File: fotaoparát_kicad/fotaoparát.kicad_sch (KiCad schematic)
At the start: 43 parts, among them J1 Conn_01x01_Pin, J10 Conn_01x01_Pin, J11 Conn_01x01_Pin, J12 Conn_01x01_Pin, J13 USB_C_Receptacle_USB2.0_16P, J2 Conn_01x01_Pin, J3 Conn_01x01_Pin, J4 Conn_01x01_Pin, J5 Conn_01x01_Pin, J6 Conn_01x01_Pin, J7 Conn_01x01_Pin, J8 Conn_01x01_Pin, J9 Conn_01x01_Pin, SW1 SW_MEC_5G, SW2 SW_MEC_5G

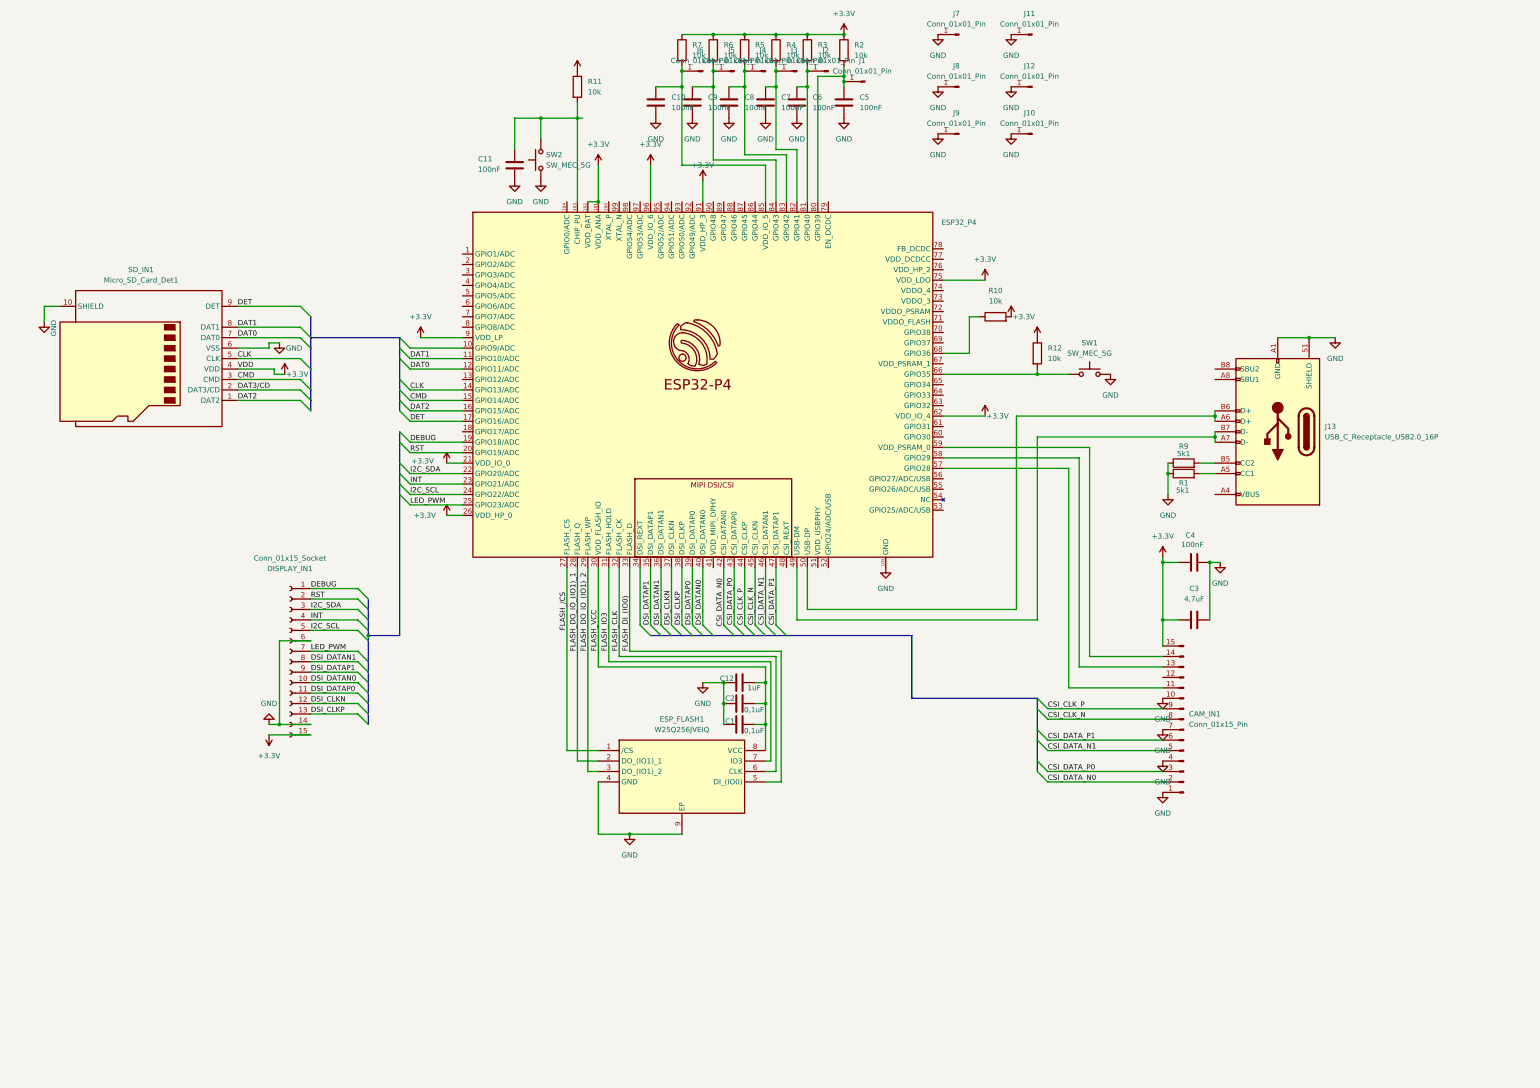
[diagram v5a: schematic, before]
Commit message: optimalizace routingu, oprava chyb, pridani baterky do soupisu mimo pcb
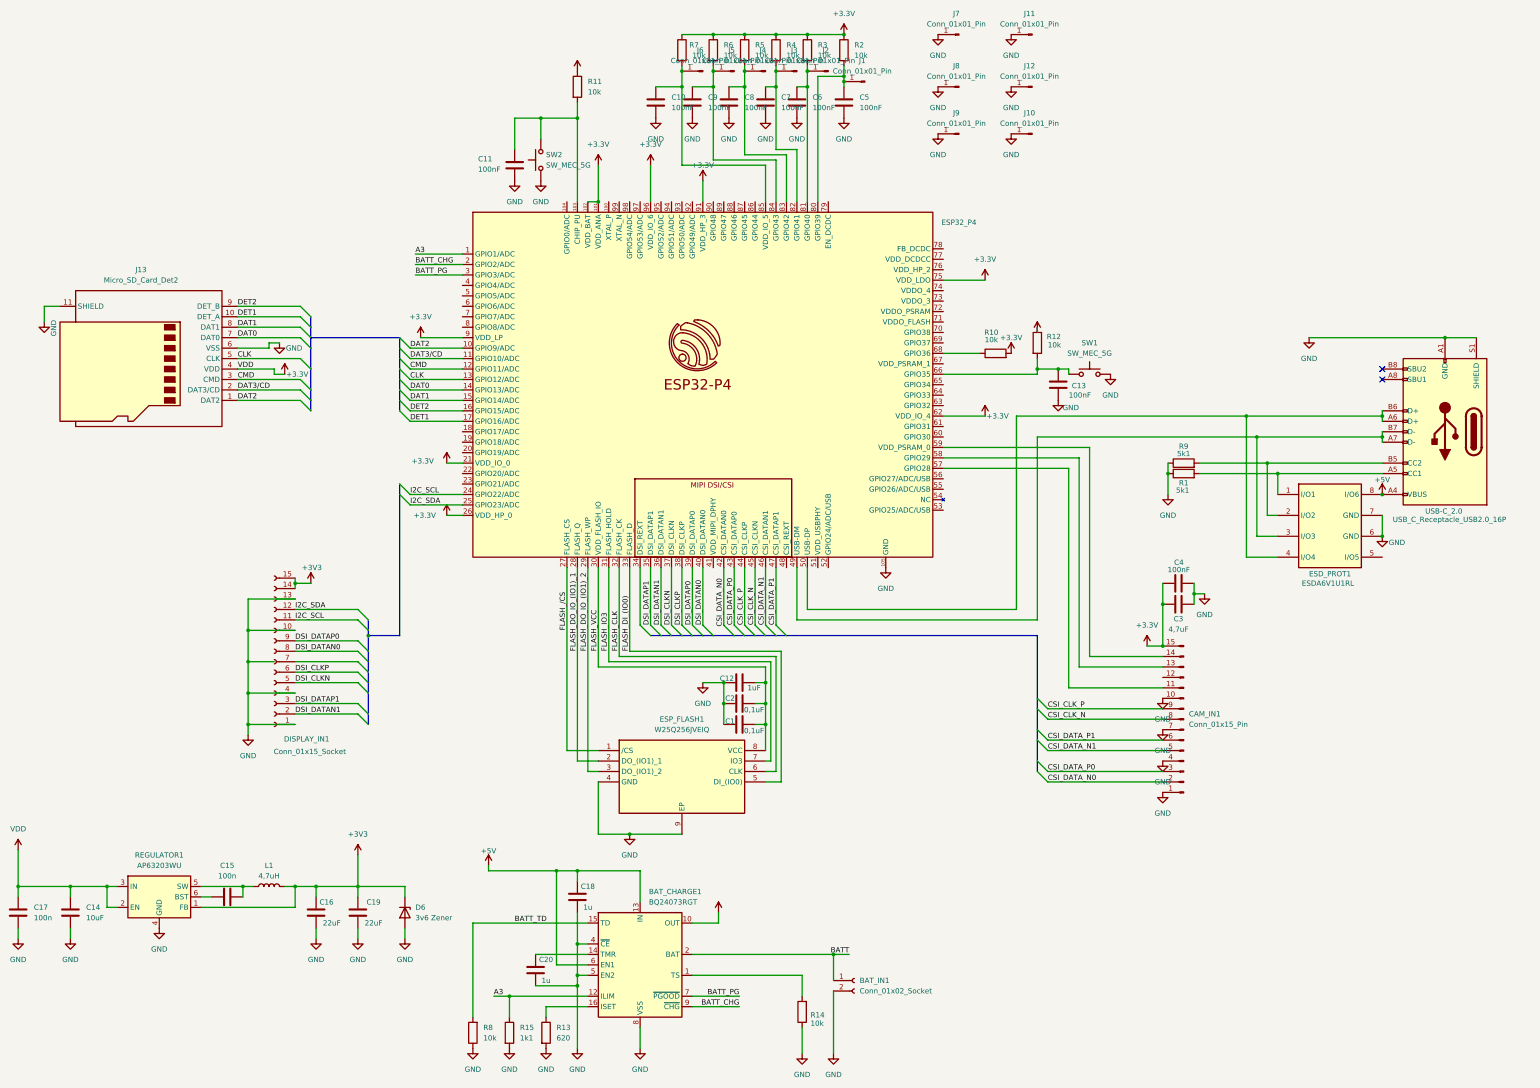
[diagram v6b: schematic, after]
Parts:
- removed SD_IN1: Micro_SD_Card_Det1, Connector_Card:SD_TE_2041021, symbol Connector:Micro_SD_Card_Det1
- added BAT_CHARGE1: BQ24073RGT, Package_DFN_QFN:VQFN-16-1EP_3x3mm_P0.5mm_EP1.6x1.6mm, symbol Battery_Management:BQ24073RGT
- added BAT_IN1: Conn_01x02_Socket, Connector_JST:JST_PH_S2B-PH-K_1x02_P2.00mm_Horizontal, symbol Connector:Conn_01x02_Socket
- added C13: 100nF, Capacitor_SMD:C_0201_0603Metric, symbol Device:C
- added C14: 10uF, Capacitor_SMD:C_0603_1608Metric, symbol Device:C
- added C15, C17: 100n, Capacitor_SMD:C_0603_1608Metric, symbol Device:C
- added C16, C19: 22uF, Capacitor_SMD:C_0603_1608Metric, symbol Device:C
- added C18, C20: 1u, Capacitor_SMD:C_0603_1608Metric, symbol Device:C
- added D6: 3v6 Zener, Diode_SMD:D_SOD-123, symbol Device:D_Zener
- added ESD_PROT1: ESDA6V1U1RL, stlib:SO-8_L4.9-W3.9-P1.27-LS5.9-BL, symbol stlib:ESDA6V1U1RL
- added J13: Micro_SD_Card_Det2, Connector_Card:microSD_HC_Hirose_DM3BT-DSF-PEJS, symbol Connector:Micro_SD_Card_Det2
- added L1: 4,7uH, stlib:IND-SMD_L3.5-W3.0, symbol Device:L
- added R13: 620, Resistor_SMD:R_0603_1608Metric, symbol Device:R
- added R14, R8: 10k, Resistor_SMD:R_0603_1608Metric, symbol Device:R
- added R15: 1k1, Resistor_SMD:R_0603_1608Metric, symbol Device:R
- added REGULATOR1: AP63203WU, Package_TO_SOT_SMD:TSOT-23-6, symbol Regulator_Switching:AP63203WU
- SW1, SW2: footprint Button_Switch_SMD:SW_MEC_5GSH9 -> Button_Switch_SMD:SW_Push_1P1T_NO_CK_KMR2
- renumbered J13 to USB-C_2.0
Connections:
- net +3.3V: now also C14.2, C17.2, J13.4 (VDD), REGULATOR1.2 (EN), REGULATOR1.3 (IN); no longer DISPLAY_IN1.15 (Pin_15)
- net CLK: now also ESP32_P4.13 (GPIO12/ADC), J13.5 (CLK); no longer ESP32_P4.14 (GPIO13/ADC)
- net CMD: now also ESP32_P4.12 (GPIO11/ADC), J13.3 (CMD); no longer ESP32_P4.15 (GPIO14/ADC)
- net DAT0: now also ESP32_P4.14 (GPIO13/ADC), J13.7 (DAT0); no longer ESP32_P4.12 (GPIO11/ADC)
- net DAT1: now also ESP32_P4.15 (GPIO14/ADC), J13.8 (DAT1); no longer ESP32_P4.11 (GPIO10/ADC)
- net DAT2: now also ESP32_P4.10 (GPIO9/ADC), J13.1 (DAT2); no longer ESP32_P4.16 (GPIO15/ADC)
- net DAT3/CD: now also ESP32_P4.11 (GPIO10/ADC), J13.2 (DAT3/CD)
- net DSI_CLKN: now also DISPLAY_IN1.5 (Pin_5); no longer DISPLAY_IN1.12 (Pin_12)
- net DSI_CLKP: now also DISPLAY_IN1.6 (Pin_6); no longer DISPLAY_IN1.13 (Pin_13)
- net DSI_DATAN0: now also DISPLAY_IN1.8 (Pin_8); no longer DISPLAY_IN1.10 (Pin_10)
- net DSI_DATAN1: now also DISPLAY_IN1.2 (Pin_2); no longer DISPLAY_IN1.8 (Pin_8)
- net DSI_DATAP0: now also DISPLAY_IN1.9 (Pin_9); no longer DISPLAY_IN1.11 (Pin_11)
- net DSI_DATAP1: now also DISPLAY_IN1.3 (Pin_3); no longer DISPLAY_IN1.9 (Pin_9)
- net GND: now also DISPLAY_IN1.1 (Pin_1), DISPLAY_IN1.10 (Pin_10), DISPLAY_IN1.13 (Pin_13), DISPLAY_IN1.4 (Pin_4), BAT_CHARGE1.17 (VSS), BAT_CHARGE1.4 (~{CE}), BAT_CHARGE1.5 (EN2), BAT_CHARGE1.8 (VSS), BAT_IN1.2 (Pin_2), C13.2, C14.1, C16.1, C17.1, C18.2, C19.1, C20.2, D6.2 (A), ESD_PROT1.6 (GND), ESD_PROT1.7 (GND), J13.11 (SHIELD), J13.6 (VSS), R13.2, R14.1, R15.2, R8.1, REGULATOR1.4 (GND); no longer DISPLAY_IN1.14 (Pin_14), DISPLAY_IN1.6 (Pin_6)
- net I2C_SCL: now also DISPLAY_IN1.11 (Pin_11); no longer DISPLAY_IN1.5 (Pin_5)
- net I2C_SDA: now also DISPLAY_IN1.12 (Pin_12), ESP32_P4.25 (GPIO23/ADC); no longer DISPLAY_IN1.3 (Pin_3), ESP32_P4.22 (GPIO20/ADC)
- net at ESP32_P4.66 (GPIO35), R12.2, SW1.1 (A)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: now also C13.1
- net A3: now reaches ESP32_P4.1 (GPIO1/ADC)
- net A3: now also BAT_CHARGE1.12 (ILIM), R15.1
- net BATT_CHG: now reaches ESP32_P4.2 (GPIO2/ADC)
- net BATT_CHG: now also BAT_CHARGE1.9 (~{CHG})
- net BATT_PG: now reaches ESP32_P4.3 (GPIO3/ADC)
- net BATT_PG: now also BAT_CHARGE1.7 (~{PGOOD})
- net at ESP32_P4.49 (USB-DM), USB-C_2.0.A7 (D-), USB-C_2.0.B7 (D-): now also ESD_PROT1.3 (I/O3)
- net at ESP32_P4.50 (USB-DP), USB-C_2.0.A6 (D+), USB-C_2.0.B6 (D+): now also ESD_PROT1.4 (I/O4)
- net +5V: now reaches USB-C_2.0.A4 (VBUS), USB-C_2.0.A9 (VBUS), USB-C_2.0.B4 (VBUS), USB-C_2.0.B9 (VBUS)
- net +5V: now also BAT_CHARGE1.13 (IN), BAT_CHARGE1.6 (EN1), C18.1, ESD_PROT1.8 (I/O6)
- net at R1.2, USB-C_2.0.A5 (CC1): now also ESD_PROT1.1 (I/O1)
- net at R9.2, USB-C_2.0.B5 (CC2): now also ESD_PROT1.2 (I/O2)
- net DEBUG: no longer names the net of ESP32_P4.19 (GPIO18/ADC)
- net DEBUG: no longer DISPLAY_IN1.1 (Pin_1)
- net DET renamed DET1
- net DET1: now also J13.10 (DET_A)
- net INT: no longer names the net of ESP32_P4.23 (GPIO21/ADC)
- net INT: no longer DISPLAY_IN1.4 (Pin_4)
- net LED_PWM: no longer names the net of DISPLAY_IN1.7 (Pin_7)
- net LED_PWM: no longer ESP32_P4.25 (GPIO23/ADC)
- net RST: no longer names the net of ESP32_P4.20 (GPIO19/ADC)
- net RST: no longer DISPLAY_IN1.2 (Pin_2)
- new net: BAT_CHARGE1.14 (TMR), C20.1
- new net: C15.1, REGULATOR1.6 (BST)
- new net: C15.2, L1.1, REGULATOR1.5 (SW)
- new net: BAT_CHARGE1.1 (TS), R14.2
- new net: BAT_CHARGE1.16 (ISET), R13.1
- new net +3V3: C16.2, C19.2, D6.1 (K), DISPLAY_IN1.14 (Pin_14), DISPLAY_IN1.15 (Pin_15), L1.2, REGULATOR1.1 (FB)
- new net 3V3: BAT_CHARGE1.10 (OUT), BAT_CHARGE1.11 (OUT)
- new net BATT: BAT_CHARGE1.2 (BAT), BAT_CHARGE1.3 (BAT), BAT_IN1.1 (Pin_1)
- new net BATT_TD: BAT_CHARGE1.15 (TD), R8.2
- new net DET2: ESP32_P4.16 (GPIO15/ADC), J13.9 (DET_B)
- no-connect marks 0 -> 2
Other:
- moved on the sheet: C3, C4, DISPLAY_IN1, R10, R12, USB-C_2.0

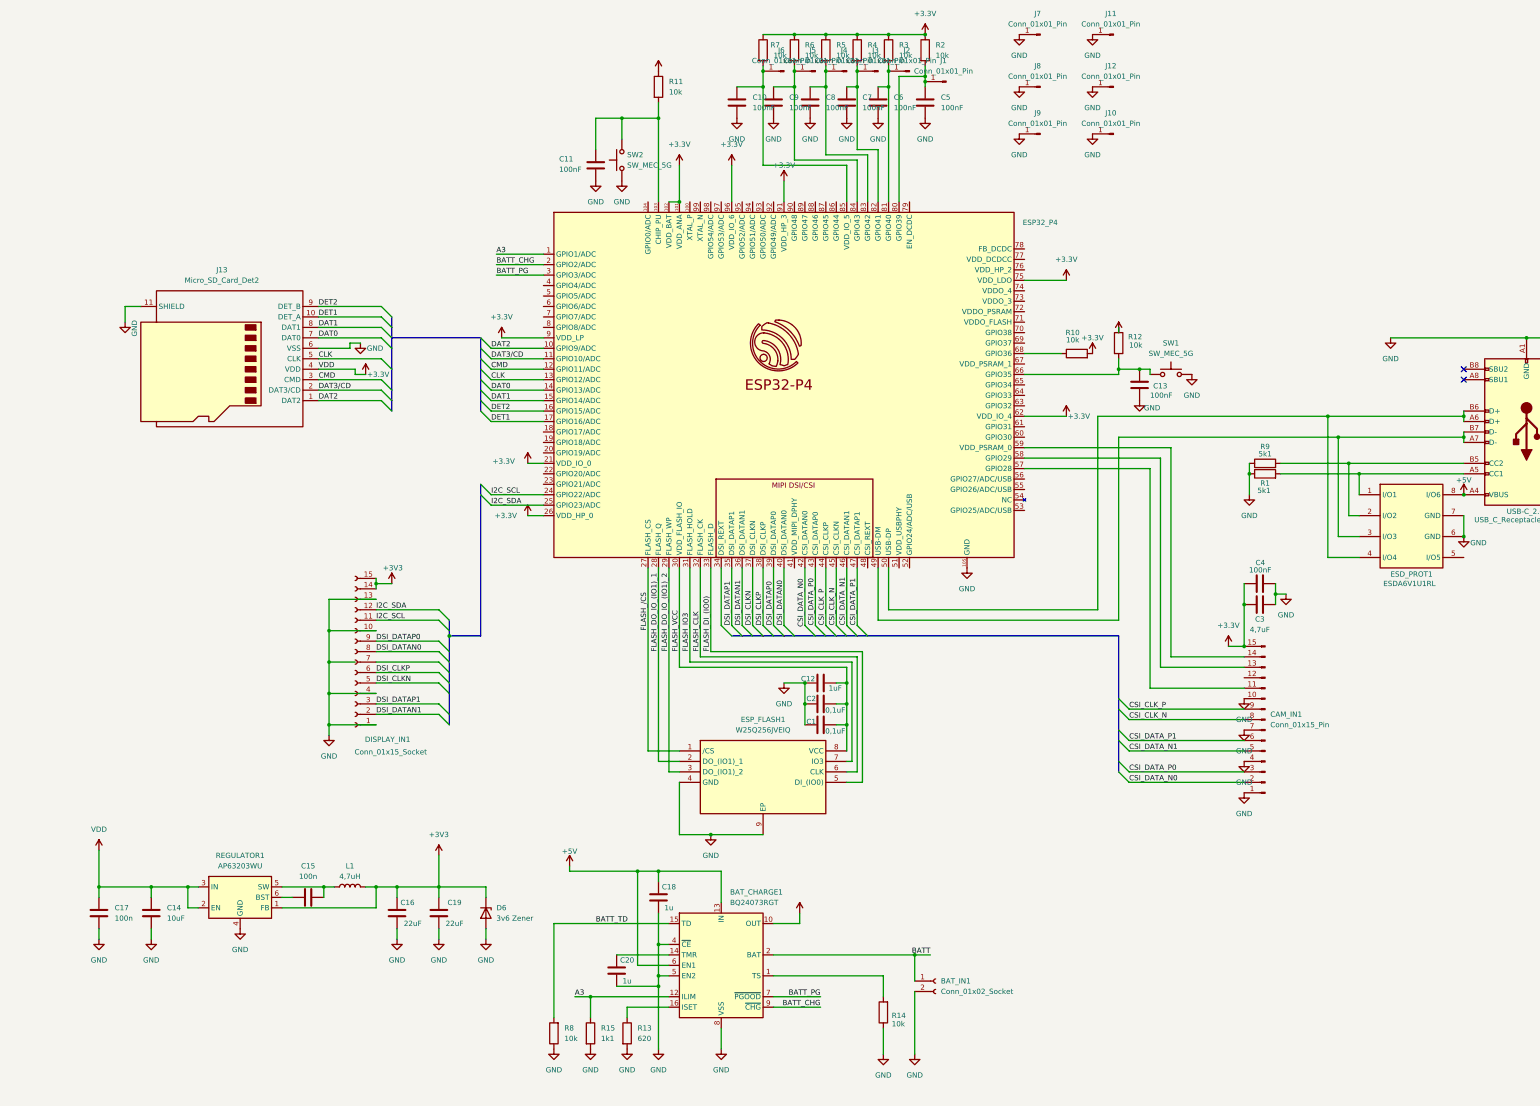
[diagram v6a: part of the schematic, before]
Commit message: Predelani 80 % routingu pro optimalizaci mista na desce, a predelani napajeni do 7,2V akumulatoru.
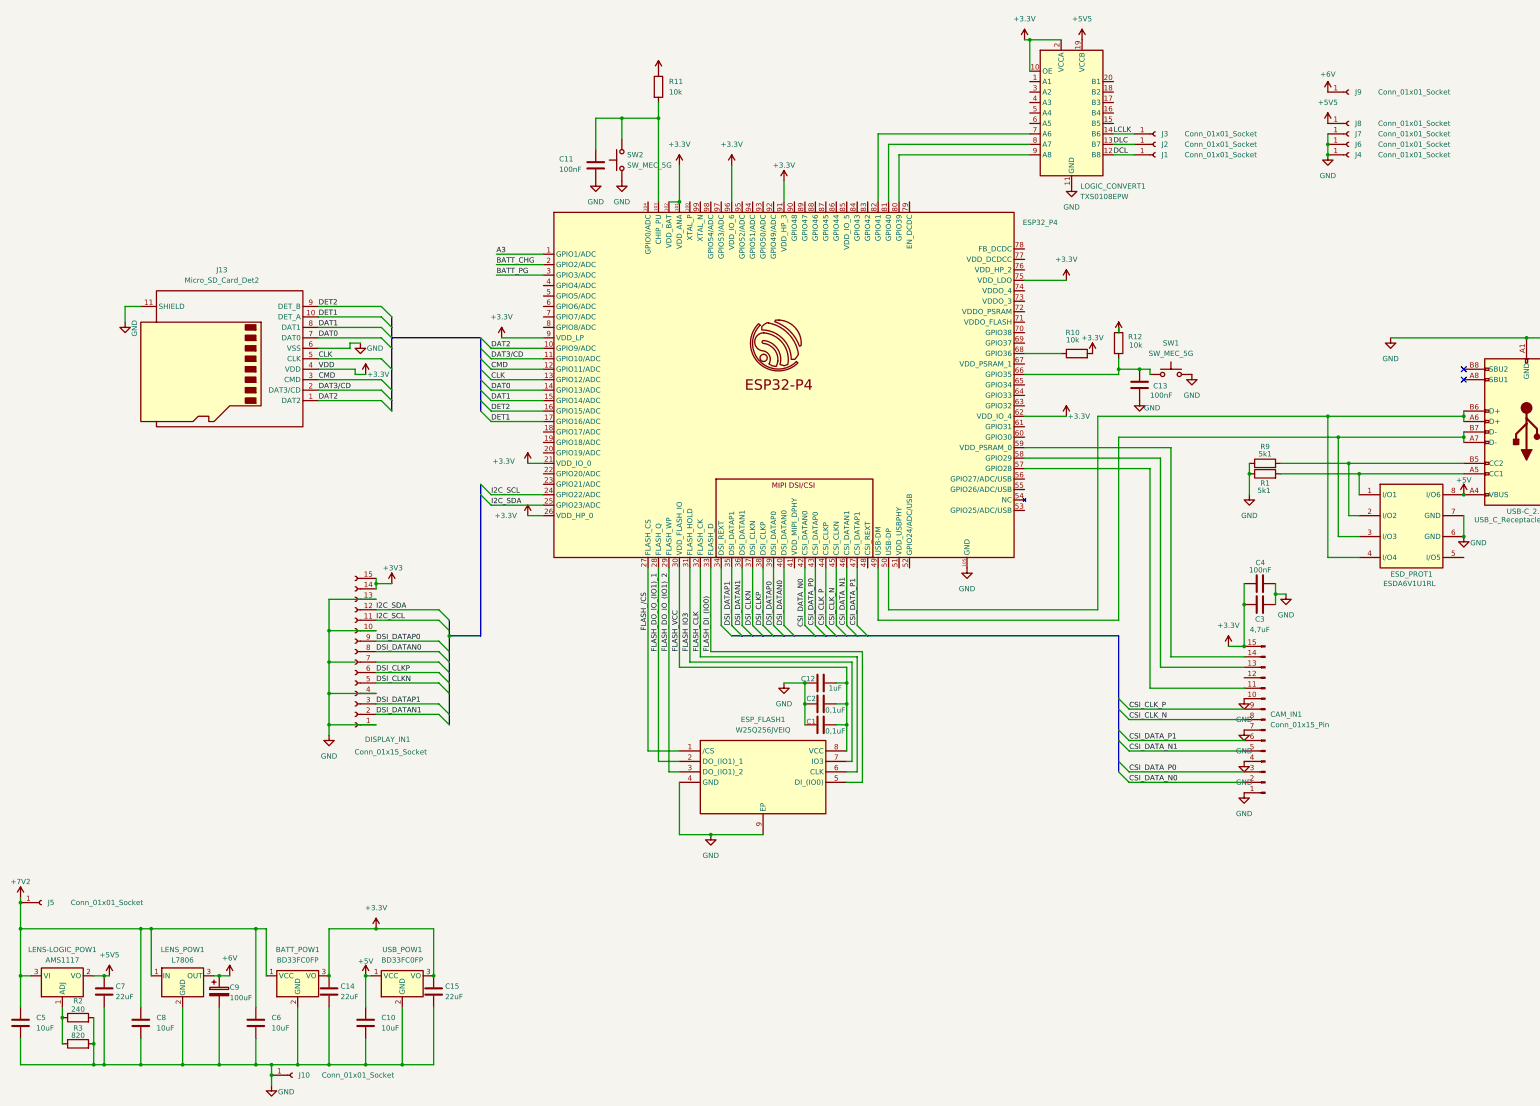
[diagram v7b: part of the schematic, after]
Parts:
- removed BAT_CHARGE1: BQ24073RGT, Package_DFN_QFN:VQFN-16-1EP_3x3mm_P0.5mm_EP1.6x1.6mm, symbol Battery_Management:BQ24073RGT
- removed BAT_IN1: Conn_01x02_Socket, Connector_JST:JST_PH_S2B-PH-K_1x02_P2.00mm_Horizontal, symbol Connector:Conn_01x02_Socket
- removed C16, C19: 22uF, Capacitor_SMD:C_0603_1608Metric, symbol Device:C
- removed C17: 100n, Capacitor_SMD:C_0603_1608Metric, symbol Device:C
- removed C18, C20: 1u, Capacitor_SMD:C_0603_1608Metric, symbol Device:C
- removed C9: 100nF, Capacitor_SMD:C_0201_0603Metric, symbol Device:C
- removed D6: 3v6 Zener, Diode_SMD:D_SOD-123, symbol Device:D_Zener
- removed J1, J10, J11, J12, J2, J3, J4, J5, J6, J7, J8, J9: Conn_01x01_Pin, Connector_Wire:SolderWire-1.5sqmm_1x01_D1.7mm_OD3.9mm, symbol Connector:Conn_01x01_Pin
- removed L1: 4,7uH, stlib:IND-SMD_L3.5-W3.0, symbol Device:L
- removed R13: 620, Resistor_SMD:R_0603_1608Metric, symbol Device:R
- removed R14, R4, R5, R6, R7, R8: 10k, Resistor_SMD:R_0603_1608Metric, symbol Device:R
- removed R15: 1k1, Resistor_SMD:R_0603_1608Metric, symbol Device:R
- removed REGULATOR1: AP63203WU, Package_TO_SOT_SMD:TSOT-23-6, symbol Regulator_Switching:AP63203WU
- added BATT_POW1, USB_POW1: BD33FC0FP, Package_TO_SOT_SMD:TO-252-2, symbol Regulator_Linear:BD33FC0FP
- added C9: 100uF, Capacitor_SMD:CP_Elec_6.3x5.4, symbol Device:C_Polarized
- added J1, J10, J2, J3, J4, J5, J6, J7, J8, J9: Conn_01x01_Socket, Connector_Wire:SolderWirePad_1x01_SMD_1.5x3mm, symbol Connector:Conn_01x01_Socket
- added LENS-LOGIC_POW1: AMS1117, Package_TO_SOT_SMD:SOT-223-3_TabPin2, symbol Regulator_Linear:AMS1117
- added LENS_POW1: L7806, Package_TO_SOT_THT:TO-220-3_Horizontal_TabDown, symbol Regulator_Linear:L7806
- added LOGIC_CONVERT1: TXS0108EPW, Package_SO:TSSOP-20_4.4x6.5mm_P0.65mm, symbol Logic_LevelTranslator:TXS0108EPW
- C10, C5, C6, C8: value 100nF -> 10uF
- C14: value 10uF -> 22uF; footprint Capacitor_SMD:C_0603_1608Metric -> Capacitor_SMD:C_0201_0603Metric; LCSC C19702 -> (none); LCSC Part C19702 -> (none); Type Basic -> (none)
- C15: value 100n -> 22uF; footprint Capacitor_SMD:C_0603_1608Metric -> Capacitor_SMD:C_0201_0603Metric; LCSC C14663 -> (none); LCSC Part C14663 -> (none); Type Basic -> (none)
- C7: value 100nF -> 22uF
- R2: value 10k -> 240
- R3: value 10k -> 820
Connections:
- net +3.3V: now also C14.1, C15.1, BATT_POW1.3 (VO), LOGIC_CONVERT1.10 (OE), LOGIC_CONVERT1.2 (VCCA), USB_POW1.3 (VO); no longer C14.2, R2.1, R3.1
- net +5V: now also C10.1, USB_POW1.1 (VCC)
- net GND: now also C14.2, C15.2, R2.2, R3.2, BATT_POW1.2 (GND), C9.2, J10.1 (Pin_1), J4.1 (Pin_1), J6.1 (Pin_1), J7.1 (Pin_1), LENS_POW1.2 (GND), LOGIC_CONVERT1.11 (GND), USB_POW1.2 (GND); no longer C14.1
- net at ESP32_P4.83 (GPIO42): no longer C8.1
- net at ESP32_P4.85 (VDD_IO_5): no longer C10.1
- net at ESP32_P4.82 (GPIO41): now also LOGIC_CONVERT1.7 (A6); no longer C7.1
- new net: ESP32_P4.80 (GPIO39), LOGIC_CONVERT1.9 (A8)
- new net: ESP32_P4.81 (GPIO40), LOGIC_CONVERT1.8 (A7)
- new net: LENS-LOGIC_POW1.1 (ADJ), R2.1, R3.1
- new net +5V5: C7.1, J8.1 (Pin_1), LENS-LOGIC_POW1.2 (VO), LOGIC_CONVERT1.19 (VCCB)
- new net +6V: C9.1, J9.1 (Pin_1), LENS_POW1.3 (OUT)
- new net +7V2: BATT_POW1.1 (VCC), C5.1, C6.1, C8.1, J5.1 (Pin_1), LENS-LOGIC_POW1.3 (VI), LENS_POW1.1 (IN)
- new net DCL: J1.1 (Pin_1), LOGIC_CONVERT1.12 (B8)
- new net DLC: J2.1 (Pin_1), LOGIC_CONVERT1.13 (B7)
- new net LCLK: J3.1 (Pin_1), LOGIC_CONVERT1.14 (B6)
